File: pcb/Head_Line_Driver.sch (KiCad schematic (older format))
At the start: 8 parts

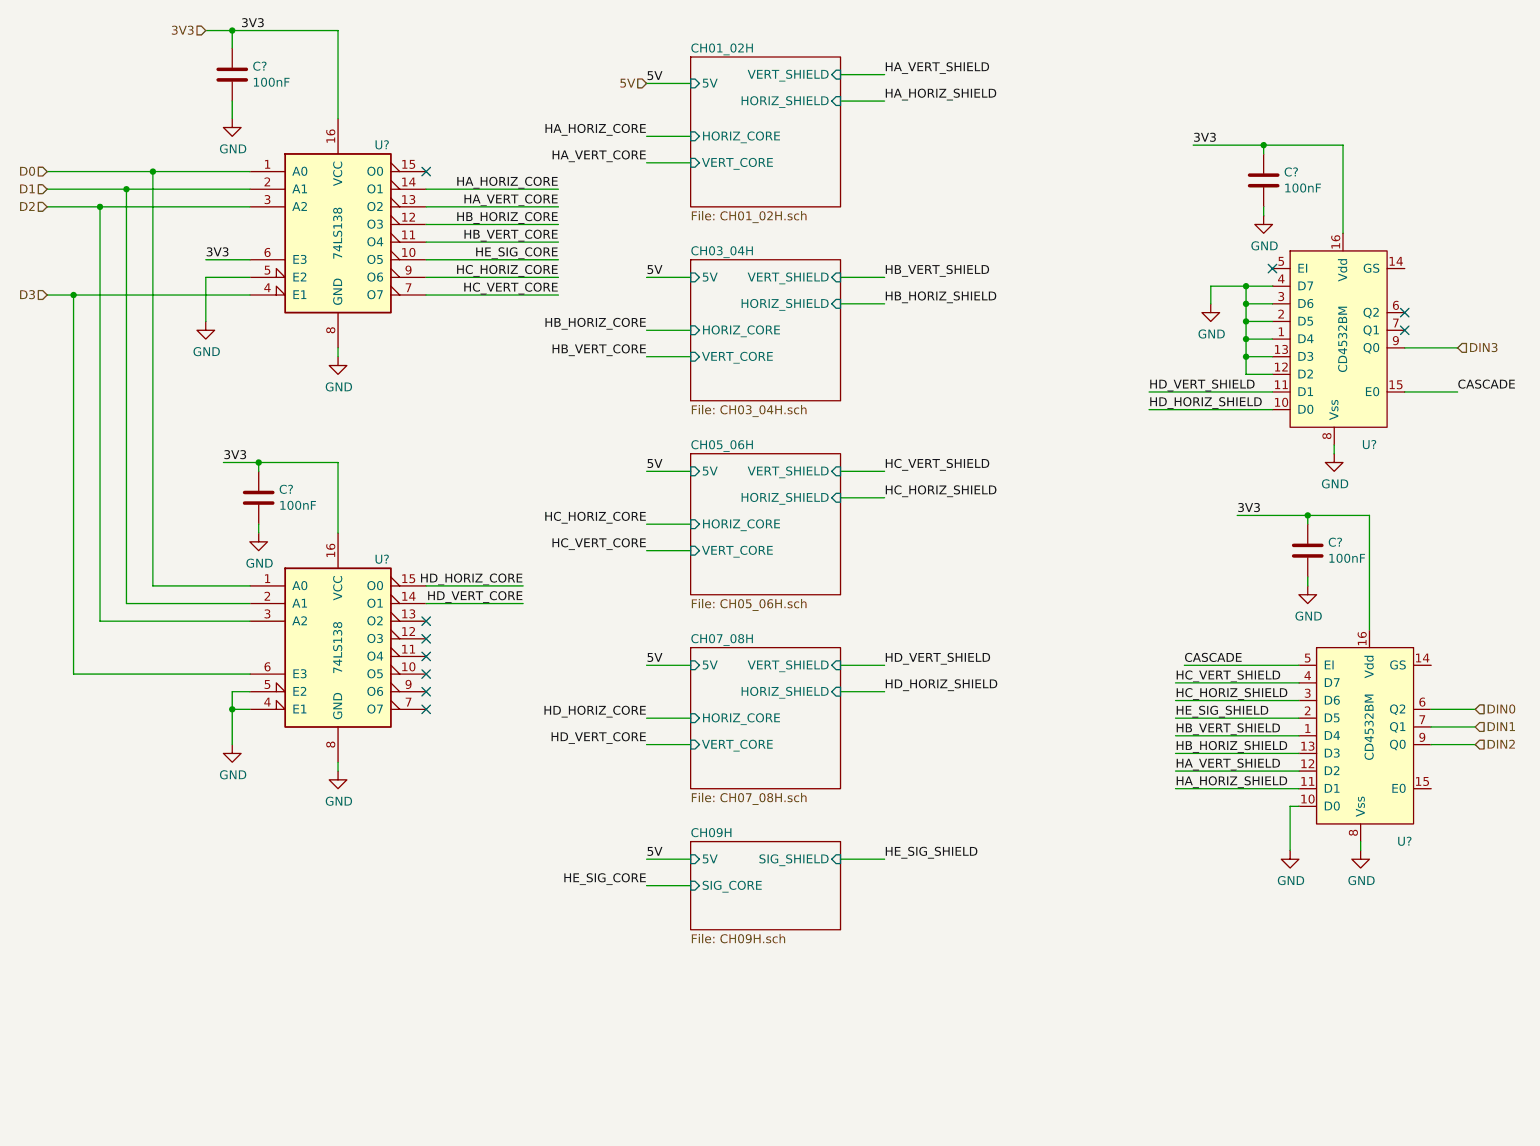
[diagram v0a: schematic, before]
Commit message: Completes first cut of the schematic
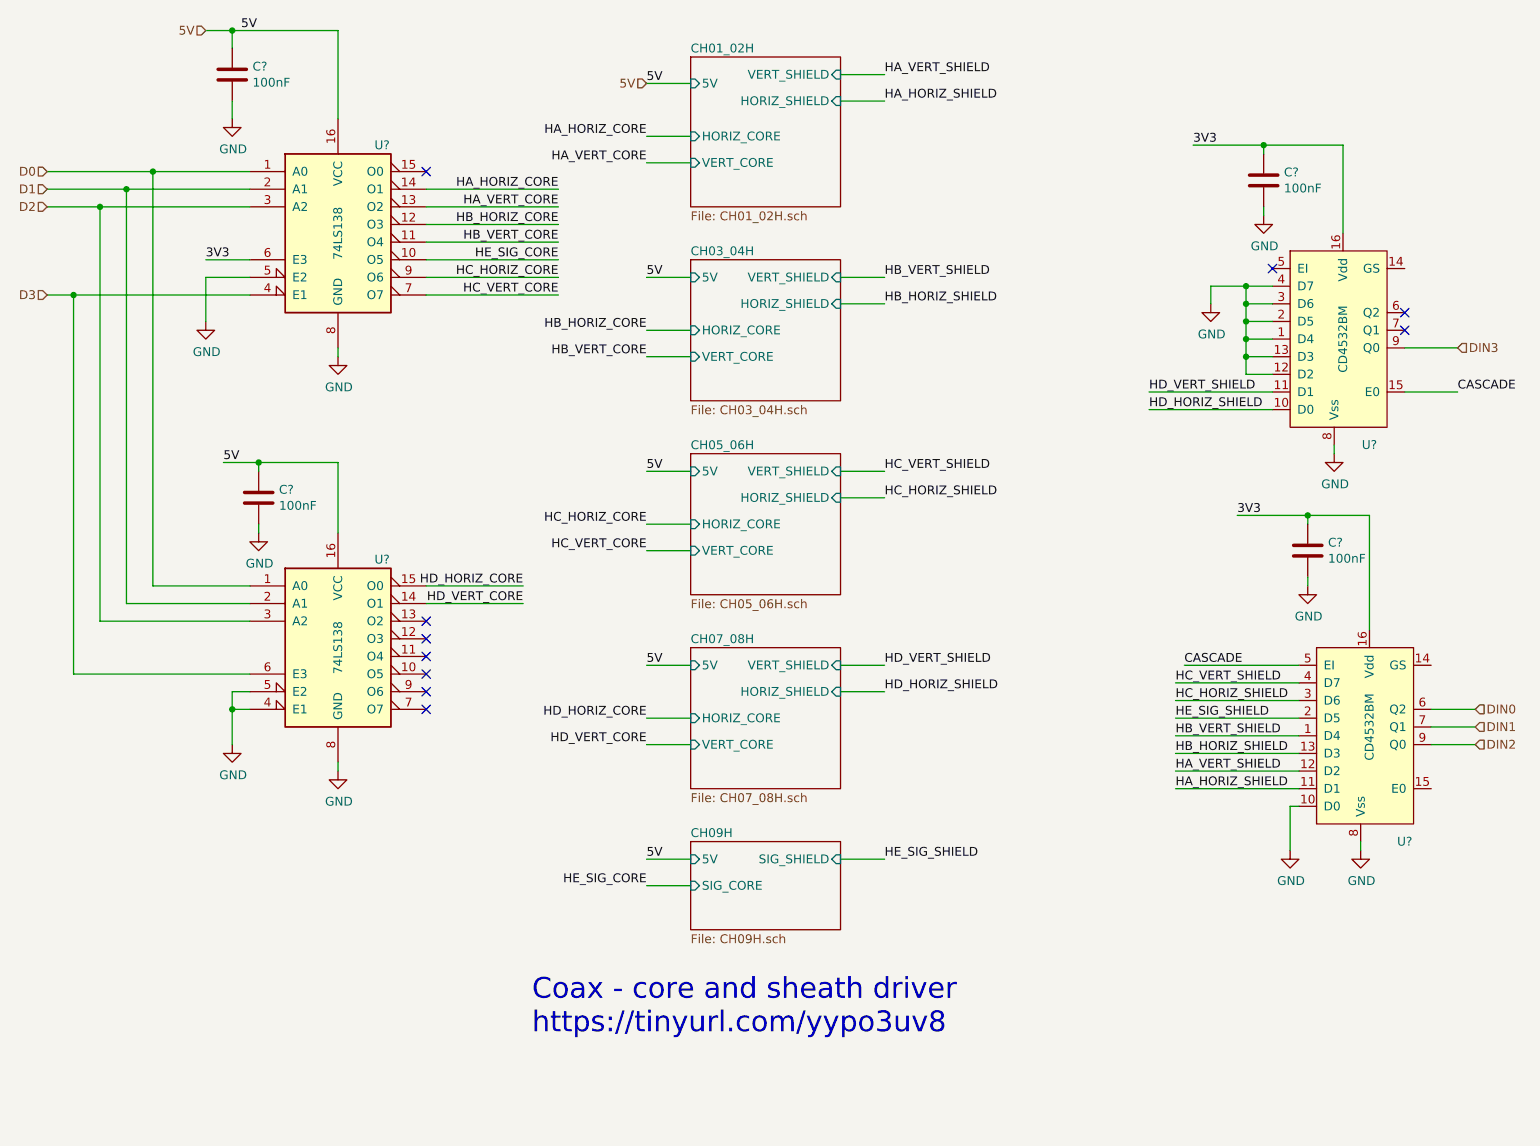
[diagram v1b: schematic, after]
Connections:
- net 3V3: no longer C?.1, C?.1, U?.16 (VCC), U?.16 (VCC)
- net 5V: now also C?.1, C?.1, U?.16 (VCC), U?.16 (VCC)
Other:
- note added: "Coax - core and sheath driver\nhttps://tinyurl.com/yypo3uv8"

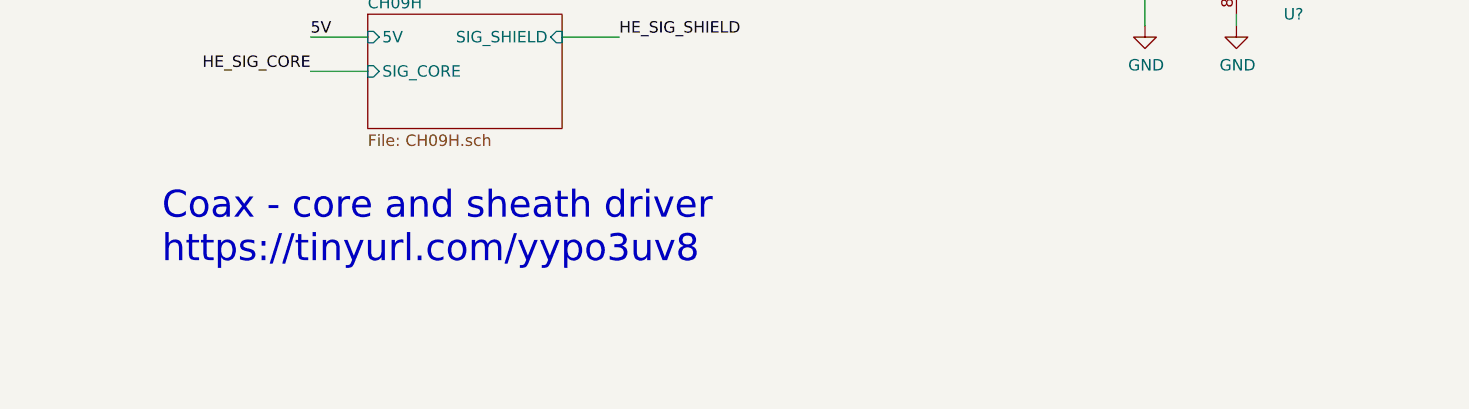
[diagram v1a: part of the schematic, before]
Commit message: Updates a comment
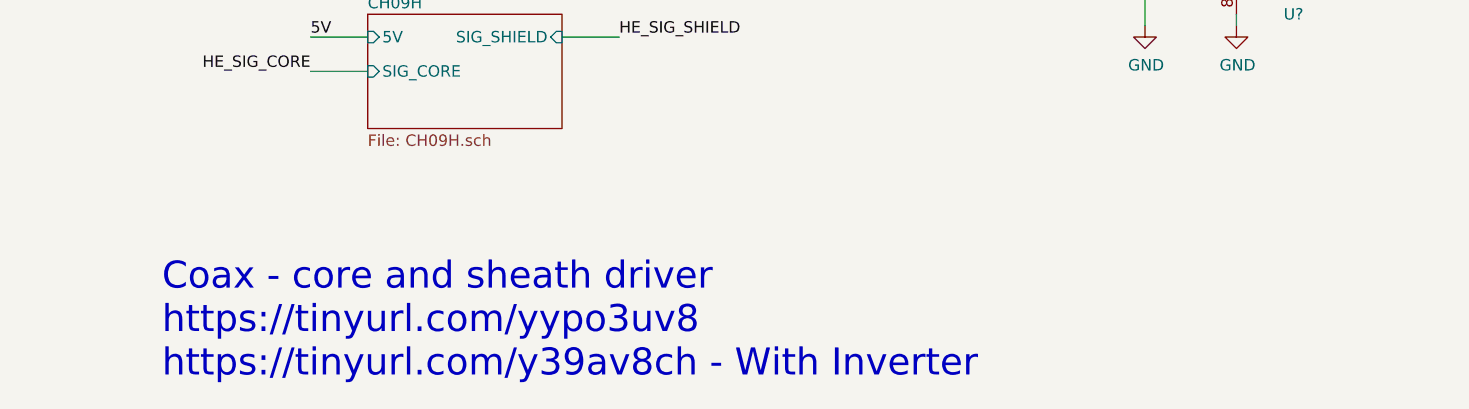
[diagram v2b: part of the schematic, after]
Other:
- note added: "Coax - core and sheath driver\nhttps://tinyurl.com/yypo3uv8\nhttps://tinyurl.com/y39av8ch - With Inverter"
- note removed: "Coax - core and sheath driver\nhttps://tinyurl.com/yypo3uv8"
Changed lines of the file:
@@
 	11050 3750 11350 3750
 NoConn ~ 10300 3050
-Text Notes 6100 7400 0    118  ~ 0
-Coax - core and sheath driver\nhttps://tinyurl.com/yypo3uv8
+Text Notes 6100 7900 0    118  ~ 0
+Coax - core and sheath driver\nhttps://tinyurl.com/yypo3uv8\nhttps://tinyurl.com/y39av8ch - With Inverter
 $Bitmap
 Pos 3450 -2300
